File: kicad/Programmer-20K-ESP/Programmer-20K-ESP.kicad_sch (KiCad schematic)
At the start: 8 parts, among them J1 Conn_01x08, SW1 STATUS, U1 HiLetgo-ESP-32S

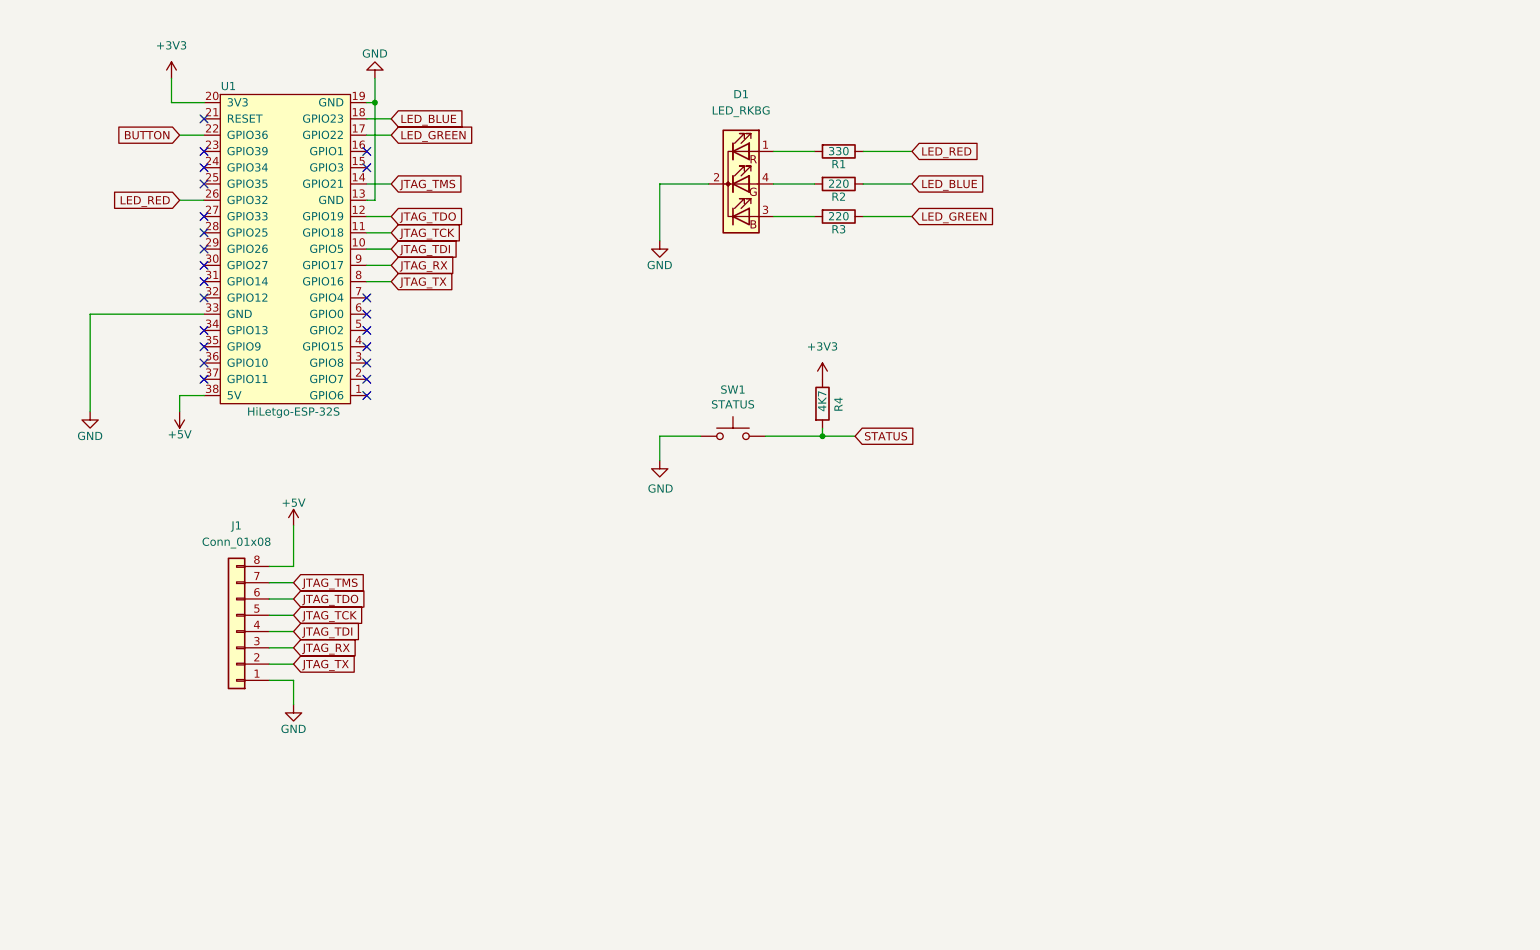
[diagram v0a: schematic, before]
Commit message: Compact PCB for the programmer
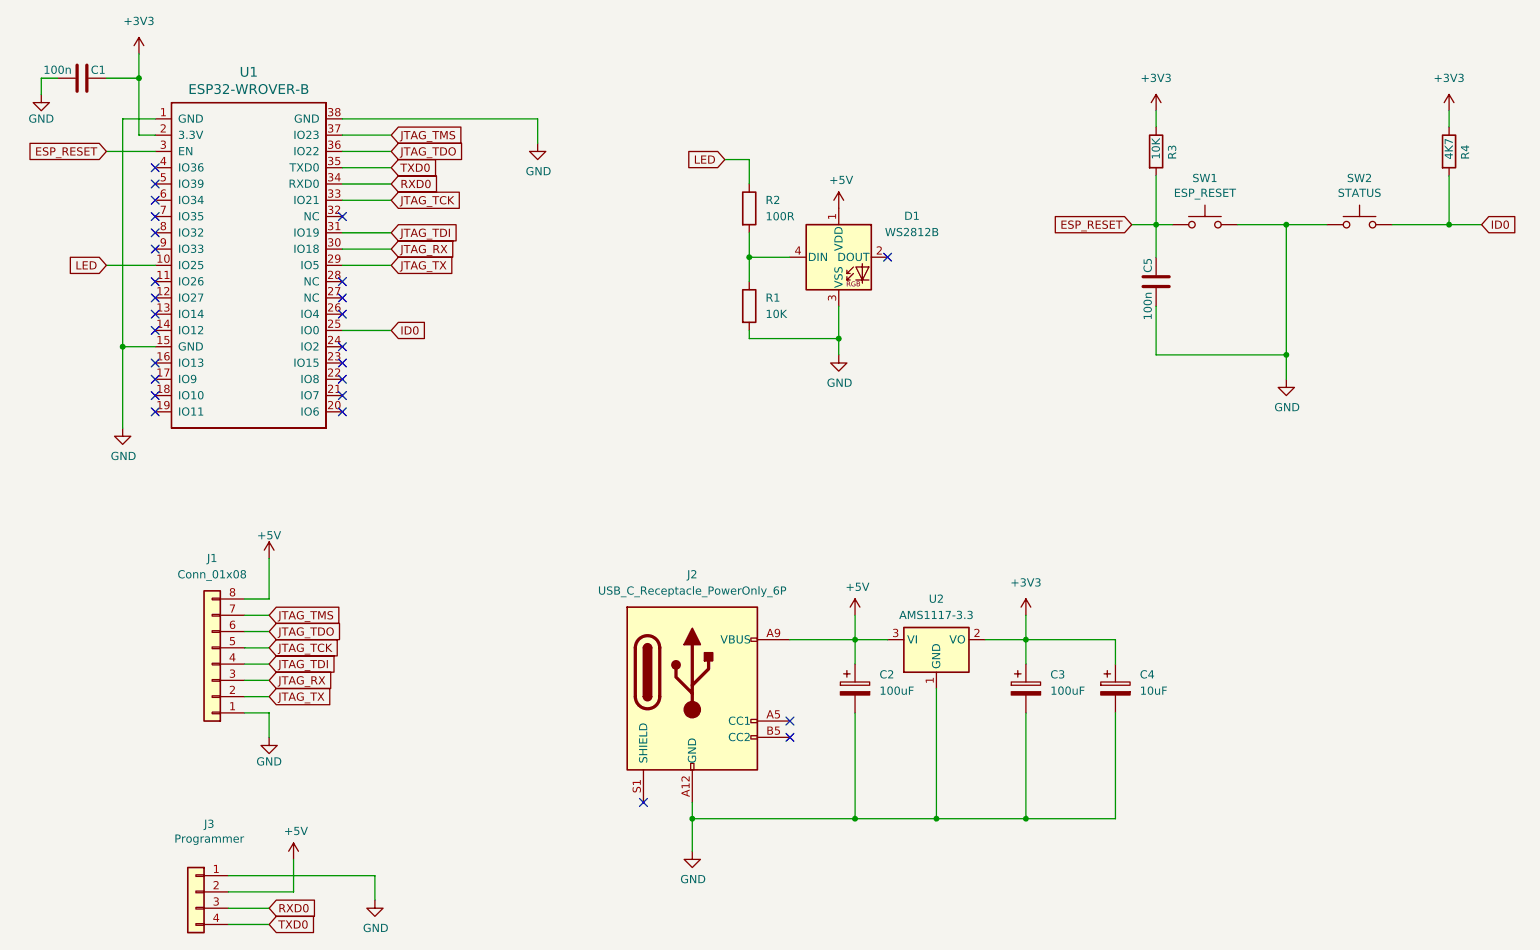
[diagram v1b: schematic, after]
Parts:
- removed D1: LED_RKBG, LED_THT:LED_D5.0mm-4_RGB, symbol Device:LED_RKBG
- removed U1: HiLetgo-ESP-32S, TRS-IO-M1:DIP-38_W22.9mm, symbol ESP-AP:HiLetgo-ESP-32S
- added C1, C5: 100n, Capacitor_SMD:C_0805_2012Metric_Pad1.18x1.45mm_HandSolder, symbol Device:C
- added C2, C3: 100uF, Capacitor_SMD:C_1206_3216Metric_Pad1.33x1.80mm_HandSolder, symbol Device:C_Polarized
- added C4: 10uF, Capacitor_SMD:C_1206_3216Metric_Pad1.33x1.80mm_HandSolder, symbol Device:C_Polarized
- added D1: WS2812B, LED_SMD:LED_WS2812B_PLCC4_5.0x5.0mm_P3.2mm, symbol LED:WS2812B
- added J2: USB_C_Receptacle_PowerOnly_6P, Connector_USB:USB_C_Receptacle_GCT_USB4125-xx-x_6P_TopMnt_Horizontal, symbol Connector:USB_C_Receptacle_PowerOnly_6P
- added J3: Programmer, Connector_PinHeader_2.54mm:PinHeader_1x04_P2.54mm_Vertical, symbol Connector_Generic:Conn_01x04
- added SW2: STATUS, Button_Switch_SMD:SW_Push_1P1T_NO_E-Switch_TL3301NxxxxxG, symbol Switch:SW_Push
- added U1: ESP32-WROVER-B, esp32-wrover:ESP32-WROVER, symbol ESP32-WROVER-B:ESP32-WROVER-B
- added U2: AMS1117-3.3, Package_TO_SOT_SMD:SOT-223-3_TabPin2, symbol Regulator_Linear:AMS1117-3.3
- J1: footprint (none) -> Connector_PinHeader_2.54mm:PinHeader_1x08_P2.54mm_Vertical
- R1: value 330 -> 10K
- R2: value 220 -> 100R
- R3: value 220 -> 10K
- SW1: value STATUS -> ESP_RESET; footprint Button_Switch_THT:SW_PUSH_6mm -> Button_Switch_SMD:SW_Push_1P1T_NO_E-Switch_TL3301NxxxxxG; LCSC C722960 -> C255812
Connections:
- net LED_GREEN is gone; now on net +3V3: R3.1
- net LED_RED is gone; now on an unnamed net: R1.1
- net +3V3: now also C1.2, C3.1, C4.1, U1.2 (3.3V), U2.2 (VO)
- net +5V: now also C2.1, D1.1 (VDD), J2.A9 (VBUS), J2.B9 (VBUS), J3.2 (Pin_2), U2.3 (VI)
- net GND: now also R1.2, SW1.2, C1.1, C2.2, C3.2, C4.2, C5.1, D1.3 (VSS), J2.A12 (GND), J2.B12 (GND), J3.1 (Pin_1), SW2.1, U1.1 (GND), U1.15 (GND), U1.38 (GND), U2.1 (GND); no longer SW1.1
- net JTAG_RX: now also U1.30 (IO18)
- net JTAG_TCK: now also U1.33 (IO21)
- net JTAG_TDI: now also U1.31 (IO19)
- net JTAG_TDO: now also U1.36 (IO22)
- net JTAG_TMS: now also U1.37 (IO23)
- net JTAG_TX: now also U1.29 (IO5)
- net ESP_RESET: now reaches R3.2
- net ESP_RESET: now also SW1.1, C5.2, U1.3 (EN)
- net at R2.2: now also D1.4 (DIN)
- net LED_BLUE renamed LED
- net LED: now also U1.10 (IO25)
- net STATUS renamed ID0
- net ID0: now also SW2.2, U1.25 (IO0); no longer SW1.2
- new net RXD0: J3.3 (Pin_3), U1.34 (RXD0)
- new net TXD0: J3.4 (Pin_4), U1.35 (TXD0)
- no-connect marks 23 -> 27
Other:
- company: (none) -> Arno Puder
- moved on the sheet: J1

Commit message: Support for WS2812B RGB LED
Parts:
- added C6: 100n, Capacitor_SMD:C_0805_2012Metric_Pad1.18x1.45mm_HandSolder, symbol Device:C
- added R5, R6: 5K1, Resistor_SMD:R_0805_2012Metric_Pad1.20x1.40mm_HandSolder, symbol Device:R
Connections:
- net +5V: now also C6.1
- net GND: now also J2.S1 (SHIELD), C6.2, R5.2, R6.2
- net at J2.A5 (CC1): now also R6.1
- net at J2.B5 (CC2): now also R5.1
- no-connect marks 27 -> 24
